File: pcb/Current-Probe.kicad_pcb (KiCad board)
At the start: 2 copper layers, 30 x 60 mm, 11 parts, among them J1 M1, J2 M2, J3 IN, J4 OUT

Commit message: style: renumber the connectors
The different number order between the two connector sets triggered me...
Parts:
- renumbered H4 to H3, H3 to H4, J3 to J1, J4 to J2, J1 to J3, J2 to J4
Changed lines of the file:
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@@
     (property "ki_keywords" "connector")
     (attr through_hole)
-    (fp_text reference "J2" (at 0 0.5 90) (layer "F.SilkS") hide
+    (fp_text reference "J4" (at 0 0.5 90) (layer "F.SilkS") hide
         (effects (font (size 1 1) (thickness 0.15)))
     )
@@
     (property "ki_keywords" "connector")
     (attr through_hole)
-    (fp_text reference "J3" (at 0 0.5 90) (layer "F.SilkS") hide
+    (fp_text reference "J1" (at 0 0.5 90) (layer "F.SilkS") hide
         (effects (font (size 1 1) (thickness 0.15)))
     )
@@
     (property "ki_keywords" "mounting hole")
     (attr exclude_from_pos_files)
-    (fp_text reference "H4" (at 0 -4.2) (layer "F.SilkS") hide
+    (fp_text reference "H3" (at 0 -4.2) (layer "F.SilkS") hide
         (effects (font (size 1 1) (thickness 0.15)))
     )
@@
     (property "ki_keywords" "connector")
     (attr through_hole)
-    (fp_text reference "J1" (at 0 0.5 90) (layer "F.SilkS") hide
+    (fp_text reference "J3" (at 0 0.5 90) (layer "F.SilkS") hide
         (effects (font (size 1 1) (thickness 0.15)))
     )
@@
     (property "ki_keywords" "mounting hole")
     (attr exclude_from_pos_files)
-    (fp_text reference "H3" (at 0 -4.2) (layer "F.SilkS") hide
+    (fp_text reference "H4" (at 0 -4.2) (layer "F.SilkS") hide
         (effects (font (size 1 1) (thickness 0.15)))
     )
@@
     (property "ki_keywords" "connector")
     (attr through_hole)
-    (fp_text reference "J4" (at 0 0.5 90) (layer "F.SilkS") hide
-        (effects (font (size 1 1) (thickness 0.15)))
-    )
+    (fp_text reference "J2" (at 0 0.5 90) (layer "F.SilkS") hide
+        (effects (font (size 1 1) (thickness 0.15)))
+    )

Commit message: feat: add BNC connector
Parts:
- added J5: M, Connector_Coaxial:BNC_TEConnectivity_1478204_Vertical, F.Cu at (150.0, 118.5)
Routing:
- net /OUT: track 38.2 -> 1.80 mm, vias 8 -> 12
- net /IN: track 38.2 -> 1.80 mm

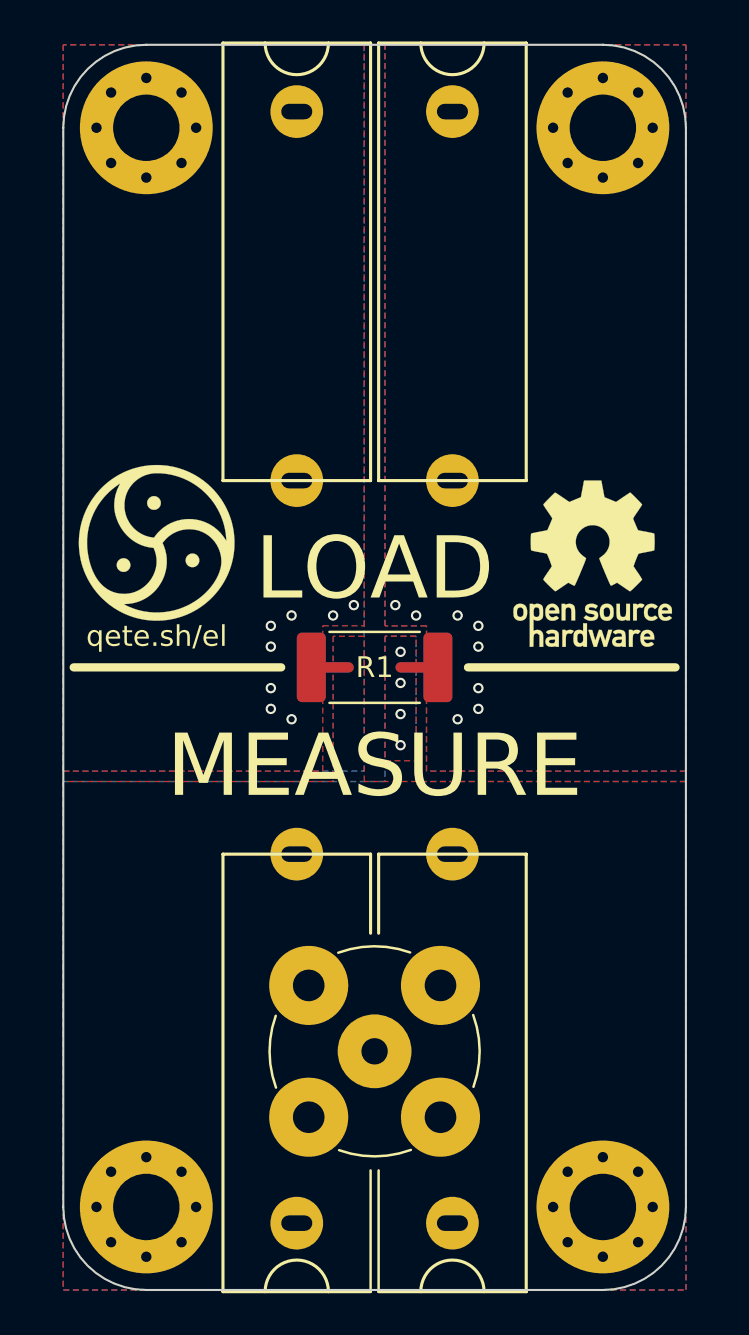
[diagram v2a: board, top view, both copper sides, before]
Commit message: feat: remove 4mm sockets on measuring side
These were not needed anymore since the board will just be used with an oscilloscope anyway. The BNC connector does the job perfectly fine...
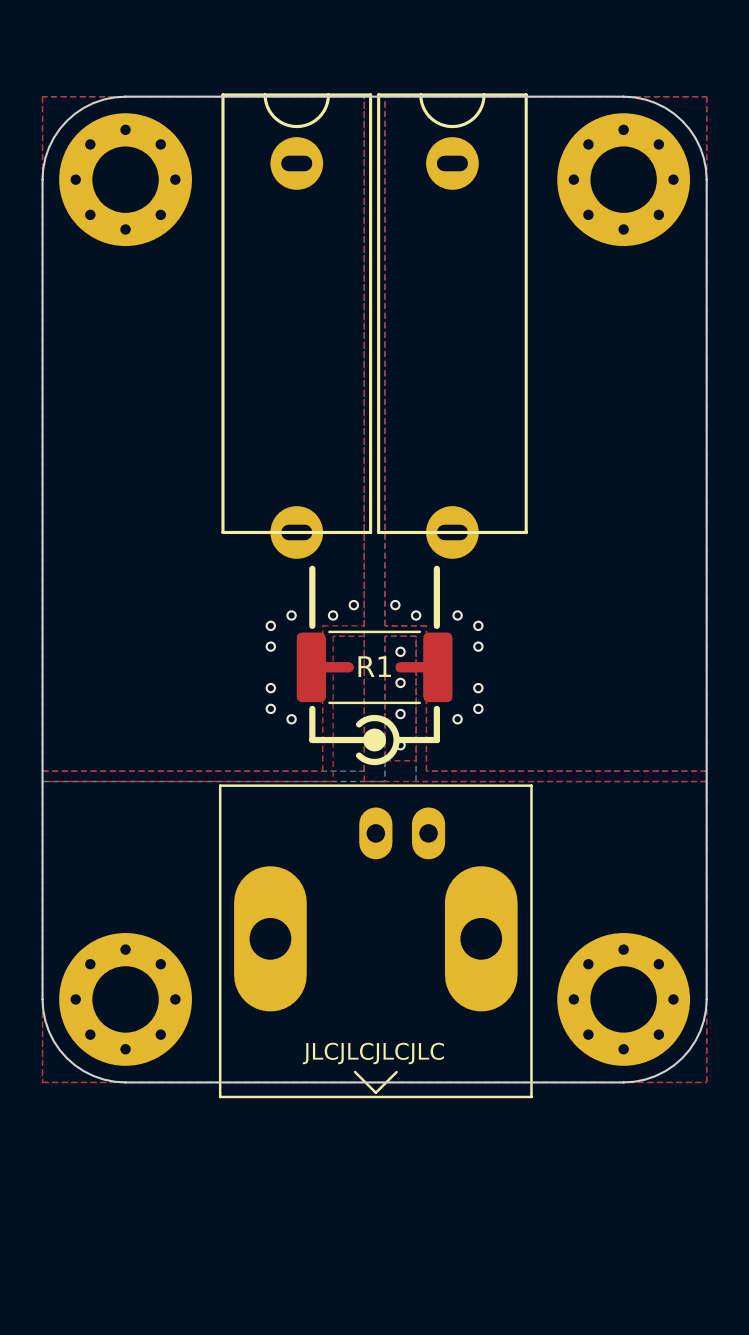
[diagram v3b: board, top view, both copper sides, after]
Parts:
- removed the J3 at (151.3, 119.2)
- removed J4: M2, My_Footprints:4mm_print_socket_with_hole
- G***, REF**: moved to B.Cu
- J3: renamed from J5; footprint Connector_Coaxial:BNC_TEConnectivity_1478204_Vertical -> Connector_Coaxial:BNC_Amphenol_B6252HB-NPP3G-50_Horizontal
- moved J3 10.5 mm to (150.1, 108.0)
- moved H3 10.0 mm to (138.0, 116.0)
- moved H4 10.0 mm to (162.0, 116.0)
- moved G*** 4.53 mm to (139.0, 98.5), turned to 180 degrees
- moved REF** 4.53 mm to (161.0, 99.5), turned to 180 degrees
- moved H1 2.69 mm to (138.0, 76.5)
- moved H2 2.69 mm to (162.0, 76.5)
- moved J1 2.50 mm to (141.2, 83.3)
- moved J2 2.50 mm to (148.7, 83.3)
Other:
- board size 30 x 60 mm -> 32 x 47.5 mm
- board text removed: "LOAD"
- board text removed: "MEASURE"
